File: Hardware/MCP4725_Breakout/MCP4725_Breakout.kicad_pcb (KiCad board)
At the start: 2 copper layers, 15.6 x 15.6 mm, 37 parts, among them J1 Conn_01x02, J2 I2C, U2 MCP4725

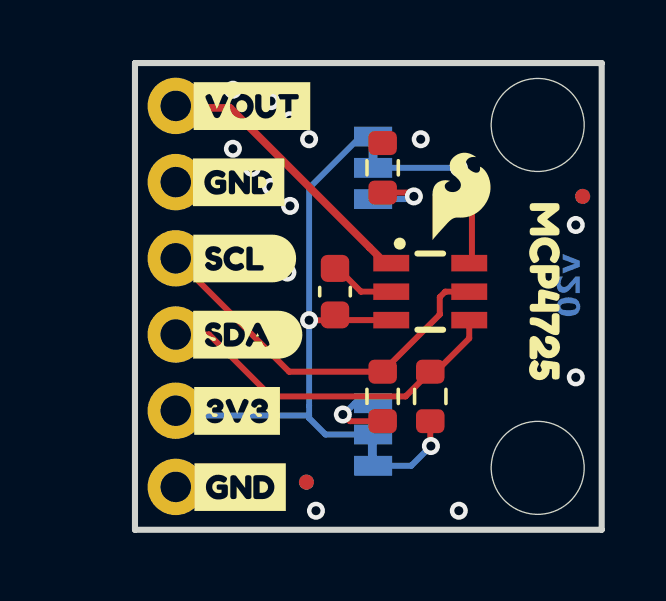
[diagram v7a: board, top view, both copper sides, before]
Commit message: Adds Qwiic Logo, power LED, adds "DAC" to product silk
* Fixes the address jumper
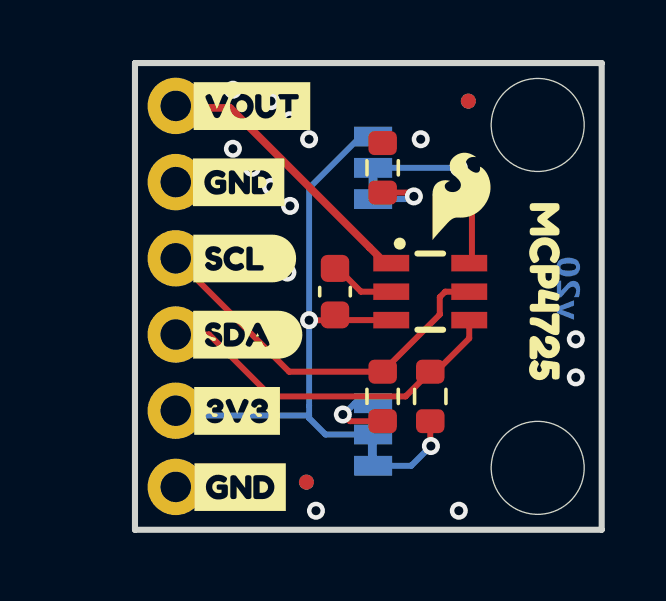
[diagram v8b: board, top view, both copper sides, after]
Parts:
- moved FID1 4.96 mm to (152.1, 98.1)
- moved FID2 4.96 mm to (152.1, 98.1)
- turned JP2 to 90 degrees
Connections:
- JP2 pad 1: 3.3V -> Net-(JP2-A)
- JP2 pad 3: Net-(JP2-C) -> 3.3V
- R1 pad 2: Net-(JP2-C) -> Net-(JP2-A)
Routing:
- net Net-(JP2-C): track 2.31 -> 0.00 mm, vias 1 -> 0
- net Net-(JP2-A): track 0.00 -> 2.31 mm, vias 0 -> 1
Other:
- board text added: "Finish: HASL Lead-Free"
- board text added: "Layers: 2"
- board text added: "Material: TG135"
- board text added: "Ordering Notes"
- board text added: "Outer Copper Weight: 1oz"
- board text added: "Silkscreen Color: White"
- board text added: "Solder Mask: Red"
- board text added: "Thickness: 1.6mm"
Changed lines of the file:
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@@
 	)
 	(paper "A4")
+	(title_block
+		(title "SparkFun I2C DAC - MCP2725")
+		(date "2026-03-18")
+		(rev "v20")
+		(company "SparkFun Electronics")
+		(comment 1 "Design By: Joel Bartlett")
+		(comment 2 "Revised By: Elias Santistevan")
+	)
 	(layers
 		(0 "F.Cu" signal)
@@
 	(net 7 "ADDR")
 	(net 8 "VOUT")
-	(net 9 "Net-(JP2-C)")
+	(net 9 "Net-(JP2-A)")
 	(footprint "SparkFun-Connector:1x04_P2.54mm"
 		(layer "F.Cu")
@@
 			(layers "F.Cu" "F.Mask" "F.Paste")
 			(roundrect_rratio 0.25)
-			(net 9 "Net-(JP2-C)")
+			(net 9 "Net-(JP2-A)")
 			(pintype "passive")
 		)
@@
 	(footprint "SparkFun-Aesthetic:Fiducial_0.5mm_Mask1mm"
 		(layer "F.Cu")
-		(at 155.8925 101.2825)
+		(at 152.0825 98.1075)
 		(descr "Circular Fiducial, 0.5mm bare copper, 1mm soldermask opening (Level C)")
 		(tags "SparkFun fiducial")
@@
 	(footprint "SparkFun-Jumper:Jumper_3_NC-1_Trace"
 		(layer "B.Cu")
-		(at 148.9075 100.33 -90)
+		(at 148.9075 100.33 90)
 		(tags "SparkFun")
 		(property "Reference" "JP2"
@@
 					(bold yes)
 				)
-				(justify bottom mirror)
+				(justify top mirror)
 			)
 		)
@@
 					(bold yes)
 				)
-				(justify top mirror)
+				(justify bottom mirror)
 			)
 		)
 		(property "Datasheet" "~"
-			(at 0 0 90)
+			(at 0 0 270)
 			(unlocked yes)
 			(layer "B.Fab")
@@
 		)
 		(property "Description" "3-pole Solder Jumper, pins 1+2 closed/bridged"
-			(at 0 0 90)
+			(at 0 0 270)
 			(unlocked yes)
 			(layer "B.Fab")
@@
 		)
 		(fp_line
-			(start -1.27 1.016)
-			(end 1.27 1.016)
+			(start 1.27 -1.016)
+			(end -1.27 -1.016)
 			(stroke
 				(width 0.1524)
@@
 		)
 		(fp_line
-			(start -1.7272 0.5588)
-			(end -1.7272 -0.5588)
+			(start 1.7272 0.5588)
+			(end 1.7272 -0.5588)
 			(stroke
 				(width 0.1524)
@@
 		)
 		(fp_line
-			(start 1.7272 0.5588)
-			(end 1.7272 -0.5588)
+			(start -1.7272 0.5588)
+			(end -1.7272 -0.5588)
 			(stroke
 				(width 0.1524)
@@
 		)
 		(fp_line
-			(start 1.27 -1.016)
-			(end -1.27 -1.016)
+			(start -1.27 1.016)
+			(end 1.27 1.016)
 			(stroke
 				(width 0.1524)
@@
 		)
 		(fp_arc
-			(start -1.27 1.016)
-			(mid -1.593289 0.882089)
-			(end -1.7272 0.5588)
+			(start 1.27 -1.016)
+			(mid 1.593289 -0.882089)
+			(end 1.7272 -0.5588)
 			(stroke
 				(width 0.1524)
@@
 		)
 		(fp_arc
-			(start 1.7272 0.5588)
-			(mid 1.593289 0.882089)
-			(end 1.27 1.016)
+			(start -1.7272 -0.5588)
+			(mid -1.593289 -0.882089)
+			(end -1.27 -1.016)
 			(stroke
 				(width 0.1524)
@@
 		)
 		(fp_arc
-			(start -1.7272 -0.5588)
-			(mid -1.593289 -0.882089)
-			(end -1.27 -1.016)
+			(start 1.7272 0.5588)
+			(mid 1.593289 0.882089)
+			(end 1.27 1.016)
 			(stroke
 				(width 0.1524)
@@
 		)
 		(fp_arc
-			(start 1.27 -1.016)
-			(mid 1.593289 -0.882089)
-			(end 1.7272 -0.5588)
+			(start -1.27 1.016)
+			(mid -1.593289 0.882089)
+			(end -1.7272 0.5588)
 			(stroke
 				(width 0.1524)
@@
 		)
 		(pad "1" smd rect
-			(at -1.0414 0 270)
+			(at -1.0414 0 90)
 			(size 0.6604 1.27)
 			(layers "B.Cu" "B.Mask")
-			(net 2 "3.3V")
+			(net 9 "Net-(JP2-A)")
 			(pinfunction "A")
 			(pintype "passive")
@@
 		)
 		(pad "2" smd rect
-			(at 0 0 270)
+			(at 0 0 90)
 			(size 0.6604 1.27)
 			(layers "B.Cu" "B.Mask")
@@
 		)
 		(pad "3" smd rect
-			(at 1.0414 0 90)
+			(at 1.0414 0 270)
 			(size 0.6604 1.27)
 			(layers "B.Cu" "B.Mask")
-			(net 9 "Net-(JP2-C)")
+			(net 2 "3.3V")
 			(pinfunction "C")
 			(pintype "passive")
@@
 	(footprint "SparkFun-Aesthetic:Fiducial_0.5mm_Mask1mm"
 		(layer "B.Cu")
-		(at 155.8925 101.2825 180)
+		(at 152.0825 98.1075 180)
 		(descr "Circular Fiducial, 0.5mm bare copper, 1mm soldermask opening (Level C)")
 		(tags "SparkFun fiducial")
@@
 	)
 	(gr_text "v20"
-		(at 155.8925 103.1875 90)
-		(layer "B.Cu")
+		(at 154.94 105.41 270)
+		(layer "B.Cu" knockout)
 		(effects
 			(font
@@
 		)
 	)
+	(gr_text "Layers: 2"
+		(at 215.533392 176.53 0)
+		(layer "Eco1.User")
+		(effects
+			(font
+				(size 1.27 1.27)
+				(thickness 0.15)
+			)
+			(justify left bottom)
+		)
+	)
+	(gr_text "Outer Copper Weight: 1oz"
+		(at 246.0625 178.435 0)
+		(layer "Eco1.User")
+		(effects
+			(font
+				(size 1.27 1.27)
+				(thickness 0.15)
+			)
+			(justify left bottom)
+		)
+	)
+	(gr_text "Ordering Notes"
+		(at 209.2325 169.545 0)
+		(layer "Eco1.User")
+		(effects
+			(font
+				(size 2 2)
+				(thickness 0.15)
+			)
+			(justify left bottom)
+		)
+	)
+	(gr_text "Silkscreen Color: White"
+		(at 215.5825 174.625 0)
+		(layer "Eco1.User")
+		(effects
+			(font
+				(size 1.27 1.27)
+				(thickness 0.15)
+			)
+			(justify left bottom)
+		)
+	)
+	(gr_text "Material: TG135"
+		(at 246.0625 174.625 0)
+		(layer "Eco1.User")
+		(effects
+			(font
+				(size 1.27 1.27)
+				(thickness 0.15)
+			)
+			(justify left bottom)
+		)
+	)
+	(gr_text "Solder Mask: Red"
+		(at 215.5825 172.72 0)
+		(layer "Eco1.User")
+		(effects
+			(font
+				(size 1.27 1.27)
+				(thickness 0.15)
+			)
+			(justify left bottom)
+		)
+	)
+	(gr_text "Thickness: 1.6mm"
+		(at 215.5825 178.435 0)
+		(layer "Eco1.User")
+		(effects
+			(font
+				(size 1.27 1.27)
+				(thickness 0.15)
+			)
+			(justify left bottom)
+		)
+	)
+	(gr_text "Finish: HASL Lead-Free"
+		(at 215.5825 180.34 0)
+		(layer "Eco1.User")
+		(effects
+			(font
+				(size 1.27 1.27)
+				(thickness 0.15)
+			)
+			(justify left bottom)
+		)
+	)
 	(segment
 		(start 149.6013 104.4575)
@@
 	)
 	(via
-		(at 155.6639 102.235)
+		(at 155.6639 106.045)
 		(size 0.6)
 		(drill 0.3)
